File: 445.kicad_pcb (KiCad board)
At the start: 2 copper layers, 100 x 100 mm, 65 parts, among them J1 Screw_Terminal_01x01, J2 Screw_Terminal_01x01, J4 POT, J5 AVR-ISP-6, Q1 Q_NPN_BCE, Q2 BT136-500, SW1 Override switch, T1 Transformer_SP_1S, U1 UCC28720D, U2 TPS71533DCKR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

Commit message: Routing done
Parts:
- moved TP5 72.6 mm to (177.8, 43.2)
- moved C5 66.9 mm to (171.9, 45.7)
- moved JP1 61.3 mm to (172.7, 63.5), turned to 180 degrees
- moved R7 57.2 mm to (172.7, 67.3)
- moved C6 55.9 mm to (179.1, 57.7), turned to 90 degrees
- moved C4 54.1 mm to (175.3, 59.2), turned to 90 degrees
- moved R10 39.1 mm to (199.4, 76.2)
- moved TP1 38.8 mm to (189.2, 71.1)
- moved D5 38.4 mm to (184.7, 66.0), turned to 180 degrees
- moved C8 37.8 mm to (196.8, 81.3), turned to -90 degrees
- moved U3 37.0 mm to (181.6, 76.2)
- moved R9 35.9 mm to (193.0, 76.2), turned to 0 degrees
- moved TP2 34.1 mm to (197.6, 97.2)
- moved locked 33.6 mm to (205.3, 96.5), turned to 0 degrees
- moved C7 32.8 mm to (183.7, 69.8), turned to 0 degrees
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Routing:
- net /Sensors/SDA: track 40.0 -> 169.4 mm, vias 1 -> 3
- net Flyback output: track 35.9 -> 148.4 mm, vias 0 -> 1
- net 3.3V linear regulator output: track 52.9 -> 150.6 mm, vias 2 -> 6
- net /Sensors/SCL: track 78.7 -> 163.3 mm, vias 0 -> 2
- net /Sensors/Echo: track 0.00 -> 76.1 mm, vias 0 -> 2
- net Net-(JP1-A): track 0.00 -> 71.3 mm
- net Net-(D3-A): track 4.82 -> 63.6 mm, vias 0 -> 3
- net /Sensors/INT: track 82.2 -> 136.4 mm, vias 3 -> 5
- net Net-(Q2-G): track 0.00 -> 43.6 mm, vias 0 -> 2
- net Vac(+): track 8.50 -> 47.2 mm, vias 0 -> 2
- net Net-(R1-Pad1): track 3.43 -> 33.1 mm, vias 0 -> 2
- net /Sensors/RESET: track 23.4 -> 53.0 mm, vias 0 -> 2
- net Net-(D4-Pad2): track 16.2 -> 45.6 mm
- net Net-(D6-A): track 0.00 -> 27.3 mm, vias 0 -> 2
- net Net-(D2-+): track 28.4 -> 5.20 mm, vias 2 -> 0
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
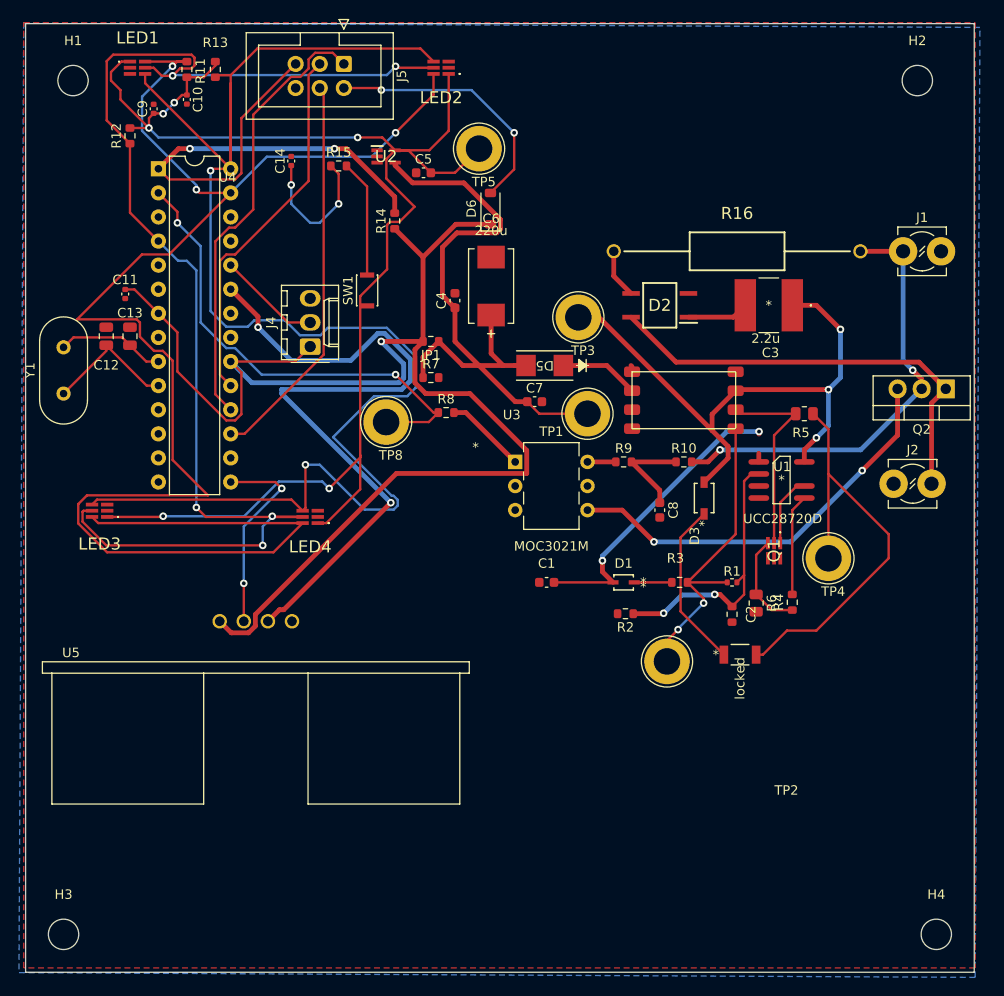
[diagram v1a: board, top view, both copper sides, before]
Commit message: Fixing DRC issues
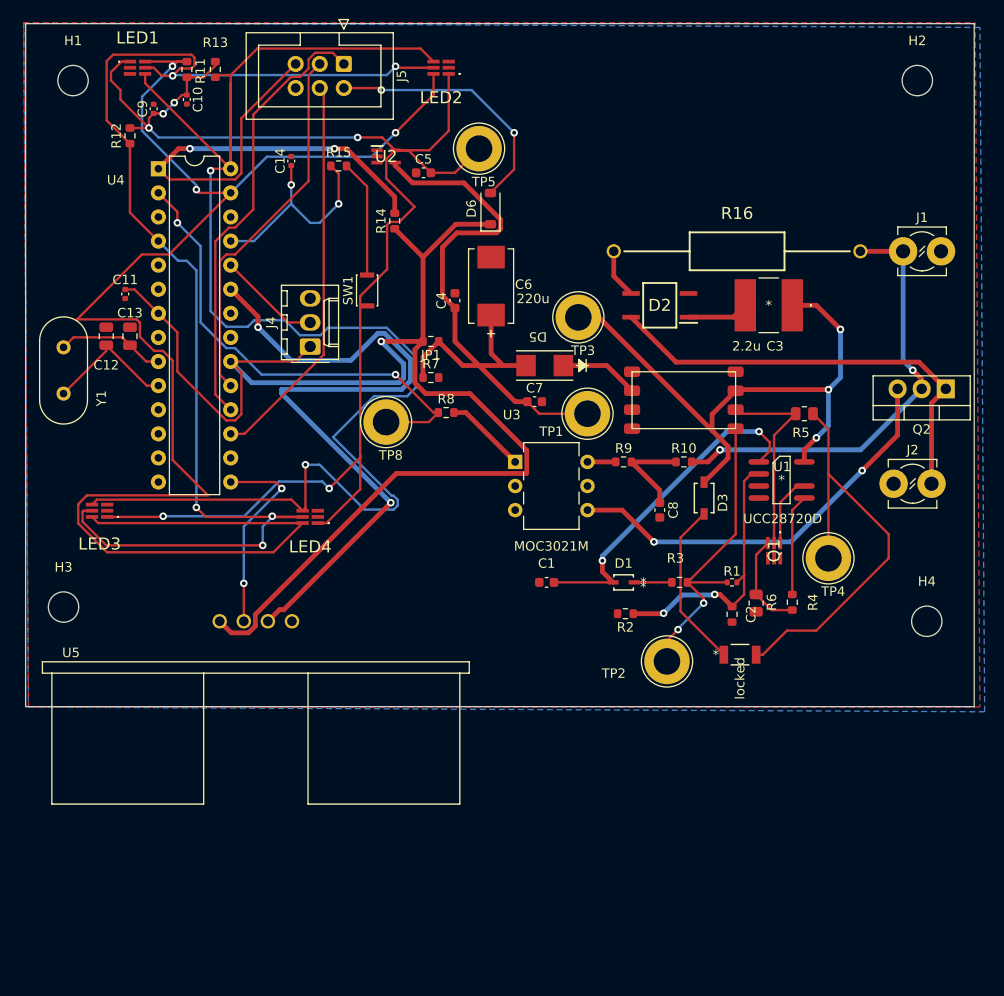
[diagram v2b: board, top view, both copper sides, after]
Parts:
- moved H3 34.5 mm to (134.0, 91.5)
- moved H4 33.0 mm to (225.0, 93.0)
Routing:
- net /Sensors/Override signal: track 15.2 -> 23.2 mm
- net Net-(D1-Output): track 32.6 -> 35.6 mm
- net Net-(JP1-A): track 71.3 -> 69.9 mm
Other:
- board size 100 x 100 mm -> 100 x 72 mm
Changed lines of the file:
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@@
     (property "ki_keywords" "quartz ceramic resonator oscillator")
     (attr through_hole)
-    (fp_text reference "Y1" (at 2.44 -3.525 90) (layer "F.SilkS")
+    (fp_text reference "Y1" (at -0.5 4 90) (layer "F.SilkS")
         (effects (font (size 1 1) (thickness 0.15)))
     )
@@
     (property "ki_keywords" "AVR 8bit Microcontroller MegaAVR PicoPower")
     (attr through_hole)
-    (fp_text reference "U4" (at 7.2875 0.906774) (layer "F.SilkS")
+    (fp_text reference "U4" (at -4.5 1.2) (layer "F.SilkS")
         (effects (font (size 1 1) (thickness 0.15)))
     )
@@
     (property "ki_keywords" "R res resistor")
     (attr smd)
-    (fp_text reference "R4" (at 0 -1.43 90) (layer "F.SilkS")
+    (fp_text reference "R4" (at -0.005 2.18 90) (layer "F.SilkS")
         (effects (font (size 1 1) (thickness 0.15)))
     )
@@
     (property "ki_keywords" "R res resistor")
     (attr smd)
-    (fp_text reference "R6" (at 0 -1.65 90) (layer "F.SilkS")
+    (fp_text reference "R6" (at -0.0825 -1.65 90) (layer "F.SilkS")
         (effects (font (size 1 1) (thickness 0.15)))
     )
@@
     (property "ki_keywords" "test point tp")
     (attr through_hole)
-    (fp_text reference "TP2" (at 12.59 13.59) (layer "F.SilkS")
+    (fp_text reference "TP2" (at -5.612 1.2688) (layer "F.SilkS")
         (effects (font (size 1 1) (thickness 0.15)))
     )
@@
   )
   (footprint "MountingHole:MountingHole_3.2mm_M3" (layer "F.Cu")
-    (at 226 126)
+    (at 225 93)
     (descr "Mounting Hole 3.2mm, no annular, M3")
     (tags "mounting hole 3.2mm no annular m3")
@@
         (effects (font (size 1 1) (thickness 0.15)))
     )
-    (fp_text user "*" (at -4.175 -1.524) (layer "F.SilkS")
-        (effects (font (size 1 1) (thickness 0.15)))
-    )
-    (fp_text user "*" (at -4.175 -1.524) (layer "F.SilkS")
-        (effects (font (size 1 1) (thickness 0.15)))
-    )
     (fp_text user "0.1in/2.54mm" (at -3.048 1.27) (layer "Cmts.User")
         (effects (font (size 1 1) (thickness 0.15)))
@@
     (property "Sheetname" "")
     (attr through_hole)
-    (fp_text reference "C3" (at -0.1795 -5) (layer "F.SilkS")
+    (fp_text reference "C3" (at -0.6565 -4.31) (layer "F.SilkS")
         (effects (font (size 1 1) (thickness 0.15)))
     )
-    (fp_text value "2.2u" (at 0.3205 -3.5) (layer "F.SilkS")
+    (fp_text value "2.2u" (at 2.3435 -4.31) (layer "F.SilkS")
         (effects (font (size 1 1) (thickness 0.15)))
     )
@@
   )
   (footprint "MountingHole:MountingHole_3.2mm_M3" (layer "F.Cu")
-    (at 134 126)
+    (at 134 91.5)
     (descr "Mounting Hole 3.2mm, no annular, M3")
     (tags "mounting hole 3.2mm no annular m3")
@@
     (property "ki_keywords" "SS110-TP")
     (attr smd)
-    (fp_text reference "D5" (at 0 0 180 unlocked) (layer "F.SilkS")
+    (fp_text reference "D5" (at 0.7215 3.04 180 unlocked) (layer "F.SilkS")
         (effects (font (size 1 1) (thickness 0.15)))
     )
@@
     (property "ki_keywords" "cap capacitor")
     (attr through_hole)
-    (fp_text reference "C6" (at 7.10565 0) (layer "F.SilkS")
+    (fp_text reference "C6" (at 0.16435 3.43) (layer "F.SilkS")
         (effects (font (size 1 1) (thickness 0.15)))
     )
-    (fp_text value "220u" (at 5.83565 0) (layer "F.SilkS")
+    (fp_text value "220u" (at -1.33565 4.43) (layer "F.SilkS")
         (effects (font (size 1 1) (thickness 0.15)))
     )
@@
     (property "ki_keywords" "diode")
     (attr smd)
-    (fp_text reference "D3" (at -4 -1 90 unlocked) (layer "F.SilkS")
+    (fp_text reference "D3" (at -0.49 1.9764 90 unlocked) (layer "F.SilkS")
         (effects (font (size 1 1) (thickness 0.15)))
     )
@@
         (effects (font (size 1 1) (thickness 0.15)))
     )
-    (fp_text user "*" (at -2.667 0 90 unlocked) (layer "F.SilkS")
-        (effects (font (size 1 1) (thickness 0.15)))
-    )
-    (fp_text user "*" (at -2.667 0 90) (layer "F.SilkS")
-        (effects (font (size 1 1) (thickness 0.15)))
-    )
     (fp_text user "${REFERENCE}" (at 0 0 90 unlocked) (layer "F.Fab")
         (effects (font (size 1 1) (thickness 0.15)))
@@
       (net 3 "Net-(D3-A)") (pinfunction "A") (pintype "passive"))
   )
-  (gr_rect (start 130 30) (end 230 130)
+  (gr_rect (start 130 30) (end 230 102)
     (stroke (width 0.1) (type default)) (fill none) (layer "Edge.Cuts"))
   (segment (start 202.6412 90.17) (end 203.2 90.17) (width 0.508) (layer "F.Cu") (net 2))
@@
   (via (at 158 47) (size 0.8) (drill 0.4) (layers "F.Cu" "B.Cu") (net 11))
   (segment (start 161 51) (end 160 51) (width 0.25) (layer "B.Cu") (net 11))
-  (segment (start 160 51) (end 158 49) (width 0.25) (layer "B.Cu") (net 11))
+  (segment (start 158.25 49.25) (end 158 49) (width 0.254) (layer "B.Cu") (net 11))
   (segment (start 158 49) (end 158 47) (width 0.25) (layer "B.Cu") (net 11))
   (segment (start 163 49) (end 161 51) (width 0.25) (layer "B.Cu") (net 11))
+  (segment (start 154.08 52.92) (end 158 49) (width 0.254) (layer "B.Cu") (net 11))
+  (segment (start 151.62 52.92) (end 154.08 52.92) (width 0.254) (layer "B.Cu") (net 11))
+  (segment (start 160 51) (end 158.25 49.25) (width 0.25) (layer "B.Cu") (net 11))
   (segment (start 192 54) (end 192 56.615) (width 0.508) (layer "F.Cu") (net 12))
   (segment (start 192 56.615) (end 193.825 58.44) (width 0.508) (layer "F.Cu") (net 12))
@@
   (segment (start 209.55 84.76) (end 209.55 80.479999) (width 0.254) (layer "F.Cu") (net 30))
   (segment (start 211.289999 78.74) (end 212.09 78.74) (width 0.254) (layer "F.Cu") (net 30))
-  (segment (start 211.1775 71.12) (end 205.275 71.12) (width 0.254) (layer "F.Cu") (net 31))
-  (segment (start 205.275 71.12) (end 204.85 70.695) (width 0.254) (layer "F.Cu") (net 31))
   (segment (start 208.9 84.76) (end 208.9 73.3975) (width 0.254) (layer "F.Cu") (net 31))
+  (segment (start 205.275 71.12) (end 211.1775 71.12) (width 0.254) (layer "F.Cu") (net 31))
+  (segment (start 204.85 70.695) (end 205.275 71.12) (width 0.254) (layer "F.Cu") (net 31))
   (segment (start 208.9 73.3975) (end 211.1775 71.12) (width 0.254) (layer "F.Cu") (net 31))
   (segment (start 208.66 91.82) (end 210.82 91.82) (width 0.254) (layer "F.Cu") (net 32))
@@
   (segment (start 176.197051 46.7868) (end 170.7896 46.7868) (width 0.508) (layer "F.Cu") (net 56))
   (segment (start 182.88 69.85) (end 184.15 71.12) (width 0.254) (layer "F.Cu") (net 56))
-  (segment (start 175.26 59.97) (end 175.26 59.69) (width 0.508) (layer "F.Cu") (net 56))
   (segment (start 179.656251 52.054) (end 180.054 51.656251) (width 0.508) (layer "F.Cu") (net 56))
   (segment (start 179.07 60.7187) (end 179.07 64.77) (width 0.508) (layer "F.Cu") (net 56))
@@
   (segment (start 182.88 69.85) (end 181.61 69.85) (width 0.508) (layer "F.Cu") (net 56))
   (segment (start 176.085 66.04) (end 173.545 63.5) (width 0.508) (layer "F.Cu") (net 56))
-  (segment (start 181.61 66.04) (end 182.753 66.04) (width 0.508) (layer "F.Cu") (net 56))
   (segment (start 182.753 66.04) (end 180.34 66.04) (width 0.508) (layer "F.Cu") (net 56))
   (segment (start 175.26 63.5) (end 177.8 66.04) (width 0.508) (layer "F.Cu") (net 56))
-  (segment (start 193.815 66.04) (end 193.93 66.155) (width 0.508) (layer "F.Cu") (net 58))
   (segment (start 186.69 66.04) (end 191.275 66.04) (width 0.508) (layer "F.Cu") (net 58))
   (segment (start 191.275 66.04) (end 193.93 68.695) (width 0.508) (layer "F.Cu") (net 58))
+  (segment (start 208.446 75.044) (end 207.29 76.2) (width 0.254) (layer "F.Cu") (net 59))
   (segment (start 191.9224 88.9) (end 185.7 88.9) (width 0.254) (layer "F.Cu") (net 59))
   (segment (start 207.29 73.0244) (end 207.3148 72.9996) (width 0.508) (layer "F.Cu") (net 59))
+  (segment (start 207.3148 72.9996) (end 208.446 74.1308) (width 0.254) (layer "F.Cu") (net 59))
   (segment (start 190.8048 86.614) (end 190.8048 87.7824) (width 0.508) (layer "F.Cu") (net 59))
-  (segment (start 207.3148 73.2654) (end 207.3148 72.9996) (width 0.508) (layer "F.Cu") (net 59))
   (segment (start 190.8048 87.7824) (end 191.9224 88.9) (width 0.508) (layer "F.Cu") (net 59))
-  (segment (start 207.29 76.2) (end 207.29 75.2986) (width 0.508) (layer "F.Cu") (net 59))
+  (segment (start 208.446 74.1308) (end 208.446 75.044) (width 0.254) (layer "F.Cu") (net 59))
   (via (at 190.8048 86.614) (size 0.8) (drill 0.4) (layers "F.Cu" "B.Cu") (net 59))
   (via (at 207.3148 72.9996) (size 0.8) (drill 0.4) (layers "F.Cu" "B.Cu") (net 59))
@@
         (xy 129.8 29.9)
         (xy 230.1 29.9)
-        (xy 230.1 129.54)
-        (xy 129.8 129.54)
+        (xy 230.6 102.04)
+        (xy 130.3 102.04)
       )
     )
@@
     (polygon
       (pts
-        (xy 230.1 130.54)
+        (xy 231.1 102.54)
         (xy 230.6 30.4)
         (xy 129.8 29.9)
-        (xy 129.3 130.04)
+        (xy 130.3 102.04)
       )
     )
